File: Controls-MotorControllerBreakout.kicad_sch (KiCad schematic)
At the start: 16 parts, among them J1 MC CAN 1, J2 MC CAN 2, J3 CAN INTRFC, J4 EXT PWR, J5 CANDAPTER, Q1 PMV35EPER

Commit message: gerbs + bom
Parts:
- J5: P/N (none) -> L77SDE09SA4CH3R
- Q1: P/N (none) -> PMV35EPER
- Z1: P/N (none) -> BZT52-B12-QX

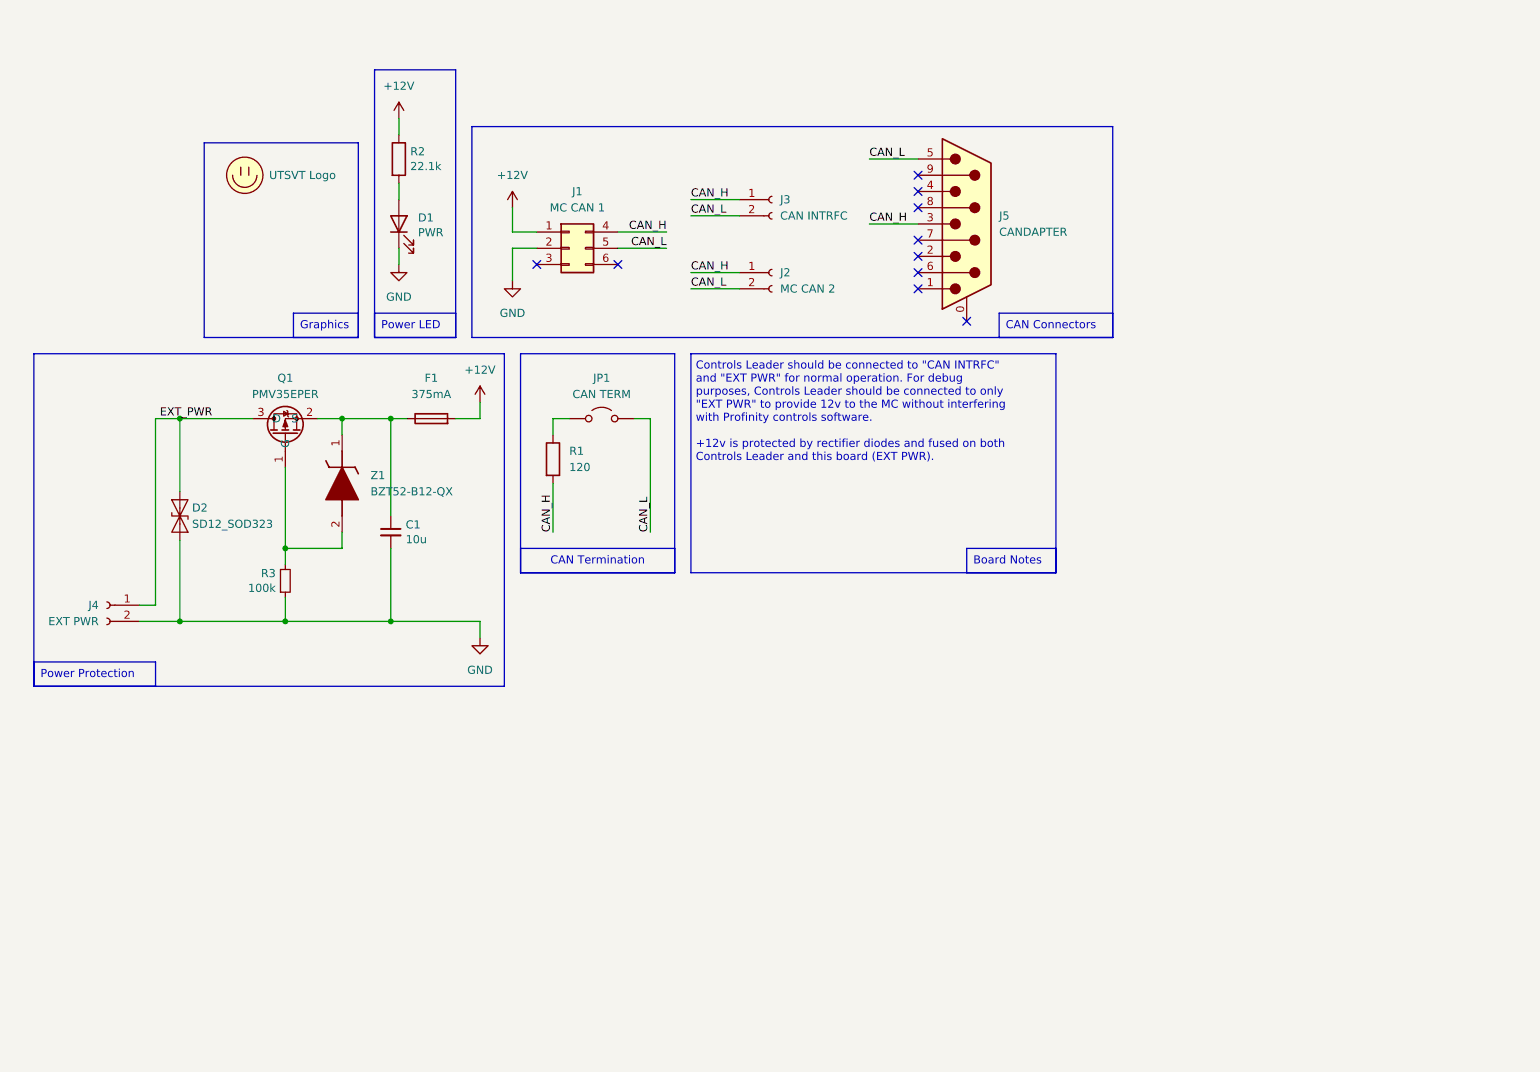
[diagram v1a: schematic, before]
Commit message: separate connector for controls
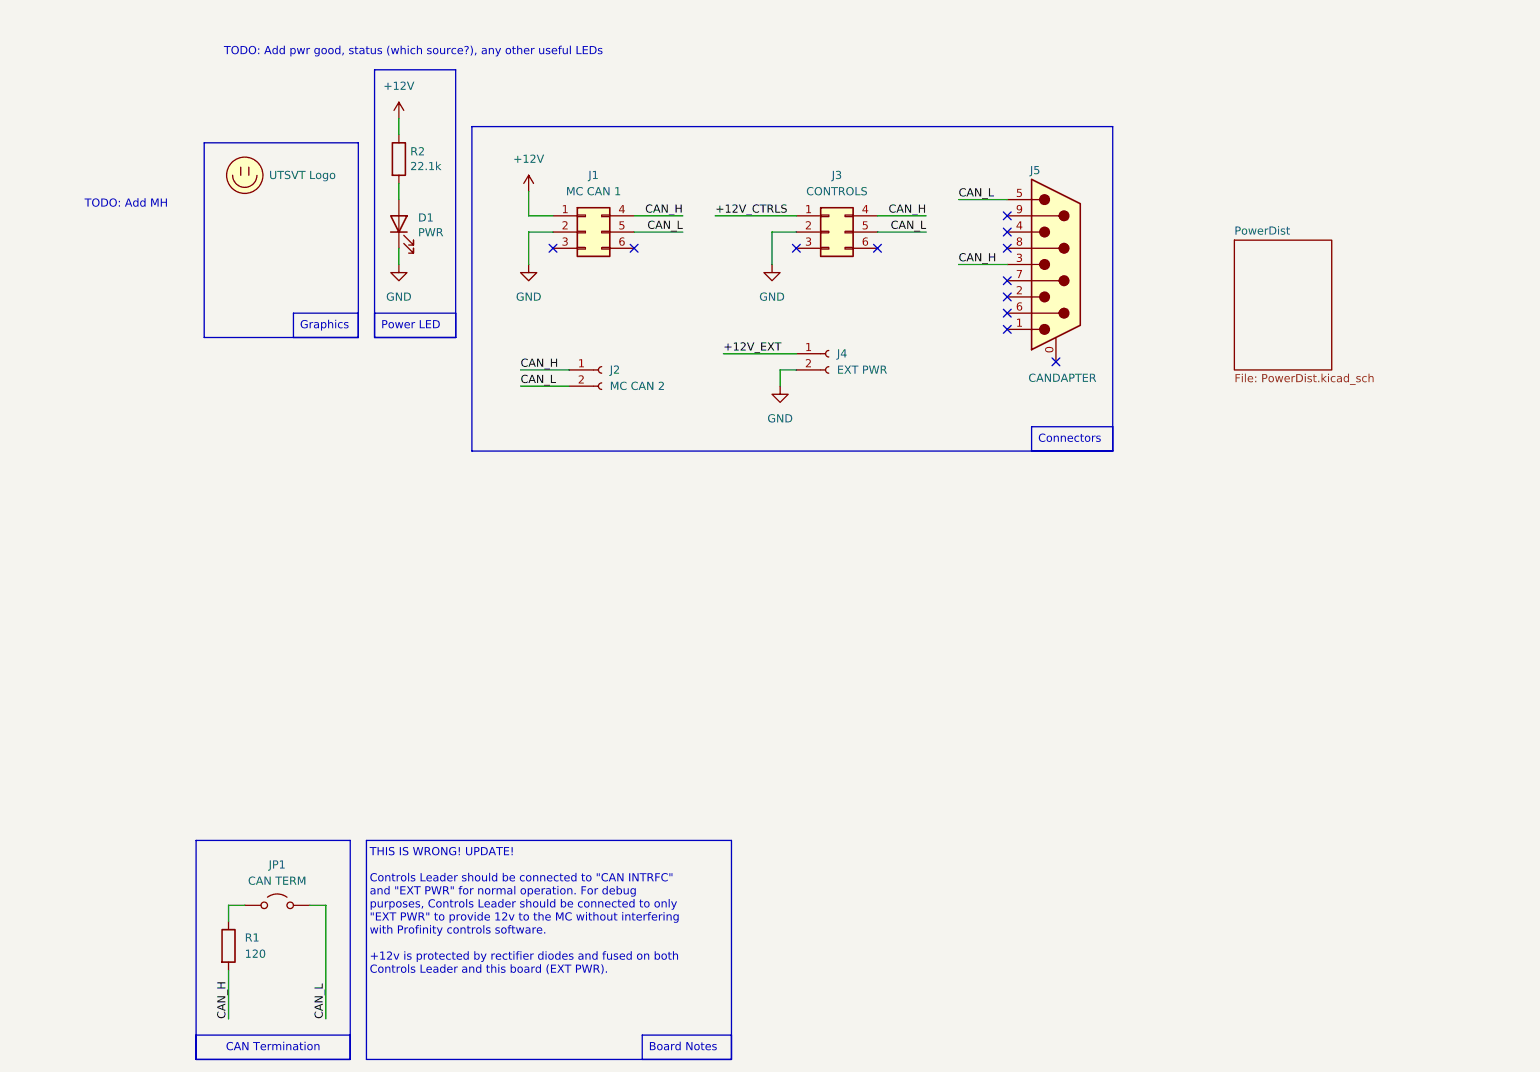
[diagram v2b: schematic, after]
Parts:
- removed C1: 10u, Capacitor_SMD:C_0805_2012Metric, symbol Device:C_Small
- removed D2: SD12_SOD323, Diode_SMD:D_SOD-323, symbol Diode:SD12_SOD323
- removed F1: 375mA, Fuse:Fuse_1206_3216Metric, symbol Device:Fuse
- removed J3: CAN INTRFC, Connector_Molex:Molex_Micro-Fit_3.0_43650-0215_1x02_P3.00mm_Vertical, symbol Connector:Conn_01x02_Socket
- removed Q1: PMV35EPER, Package_TO_SOT_SMD:SOT-23, symbol utsvt-chips:PMV35EPE
- removed R3: 100k, Resistor_SMD:R_0805_2012Metric_Pad1.20x1.40mm_HandSolder, symbol Device:R_Small
- removed Z1: BZT52-B12-QX, Zener:BZT52B12QX, symbol BZT52-B12-QX:BZT52-B12-QX
- added J3: CONTROLS, Connector_Molex:Molex_Micro-Fit_3.0_43045-0612_2x03_P3.00mm_Vertical, symbol Connector_Generic:Conn_02x03_Top_Bottom
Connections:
- net CAN_H: now also J3.4 (Pin_4)
- net CAN_L: now also J3.5 (Pin_5)
- net GND: now also J3.2 (Pin_2)
- net EXT_PWR renamed +12V_EXT
- new net +12V_CTRLS: J3.1 (Pin_1)
- no-connect marks 10 -> 12
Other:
- added sheet PowerDist (PowerDist.kicad_sch)
- note added: "THIS IS WRONG! UPDATE! Controls Leader should be connected to "CAN INTRFC" and "EXT PWR" for normal operation. For debug purposes, Controls Leader should be connected to only "EXT PWR" to provide 12v to the MC without interfering with Profinity controls software. +12v is protected by rectifier diodes and fused on both Controls Leader and this board (EXT PWR)."
- note added: "TODO: Add MH"
- note added: "TODO: Add pwr good, status (which source?), any other useful LEDs"
- note removed: "Controls Leader should be connected to "CAN INTRFC" and "EXT PWR" for normal operation. For debug purposes, Controls Leader should be connected to only "EXT PWR" to provide 12v to the MC without interfering with Profinity controls software. +12v is protected by rectifier diodes and fused on both Controls Leader and this board (EXT PWR)."
- company: (none) -> LHRS
- title: (none) -> Controls - Motor Controller Breakout
- moved on the sheet: J1, J2, J5, JP1, R1

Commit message: sch is sching (tps2121 design)
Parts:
- added H1, H2, H3, H4: MountingHole, symbol Mechanical:MountingHole
- J3: value CONTROLS -> CTRLS
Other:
- sheet PowerDist ports: added +12V_CTRLS, +12V_EXT, +12V_STATUS; removed none
- note removed: "TODO: Add MH"
- moved on the sheet: D1, R2

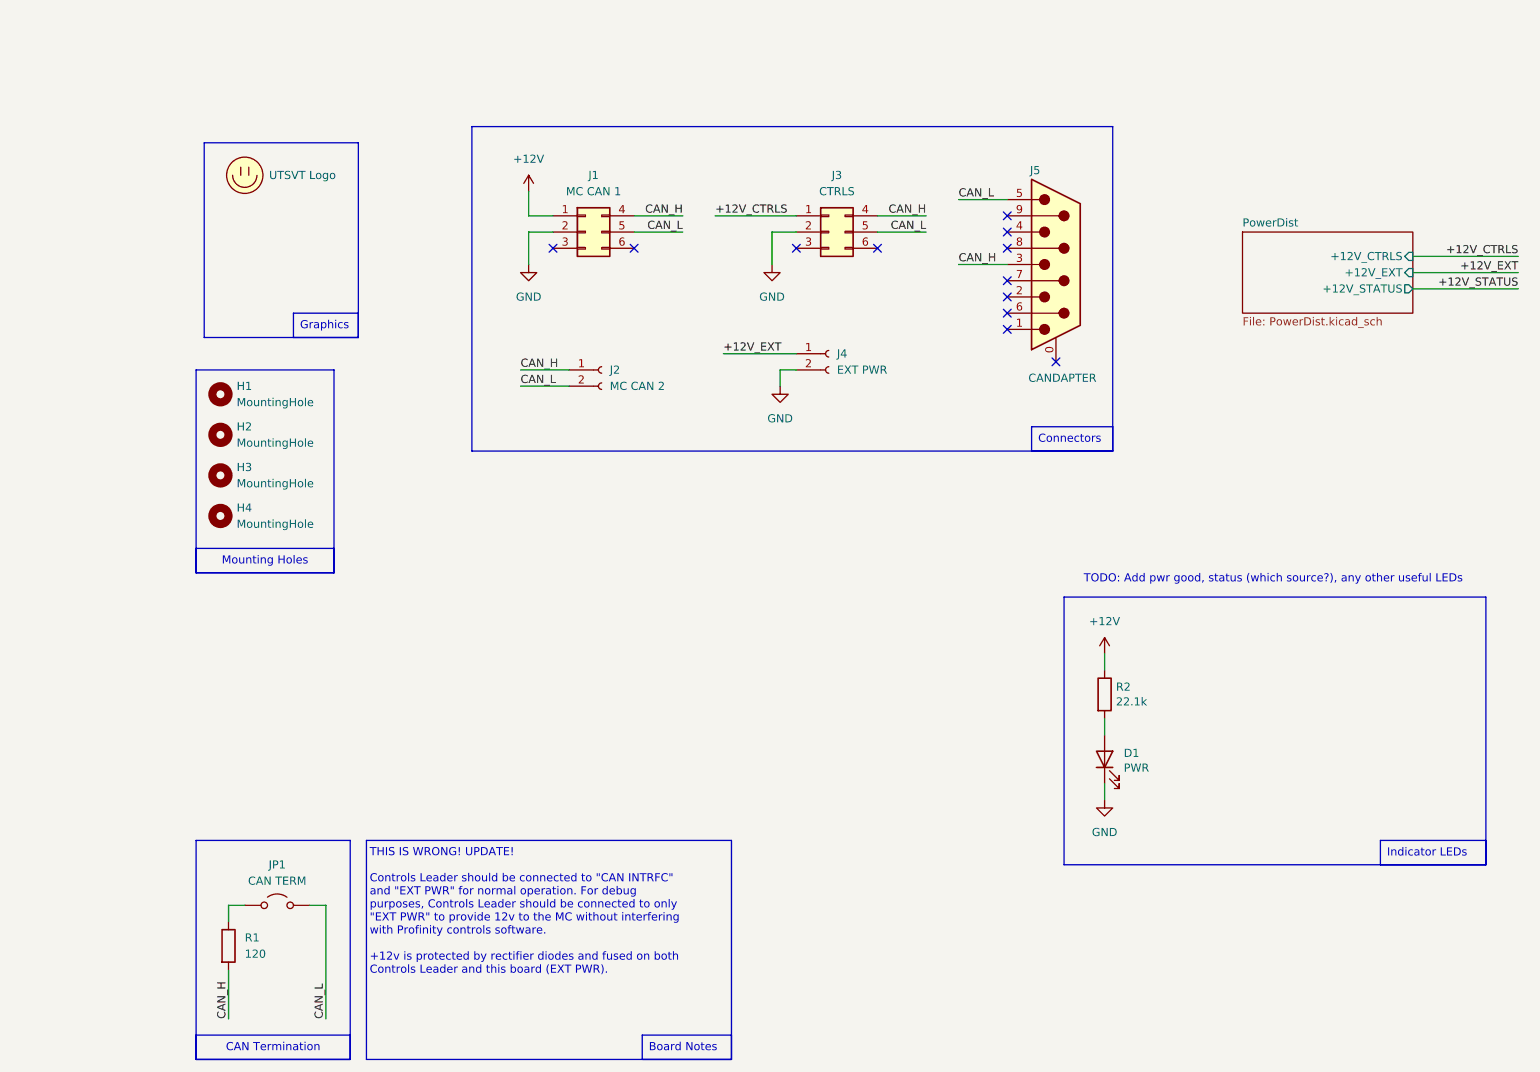
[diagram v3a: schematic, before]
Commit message: cleanup sch and add leds
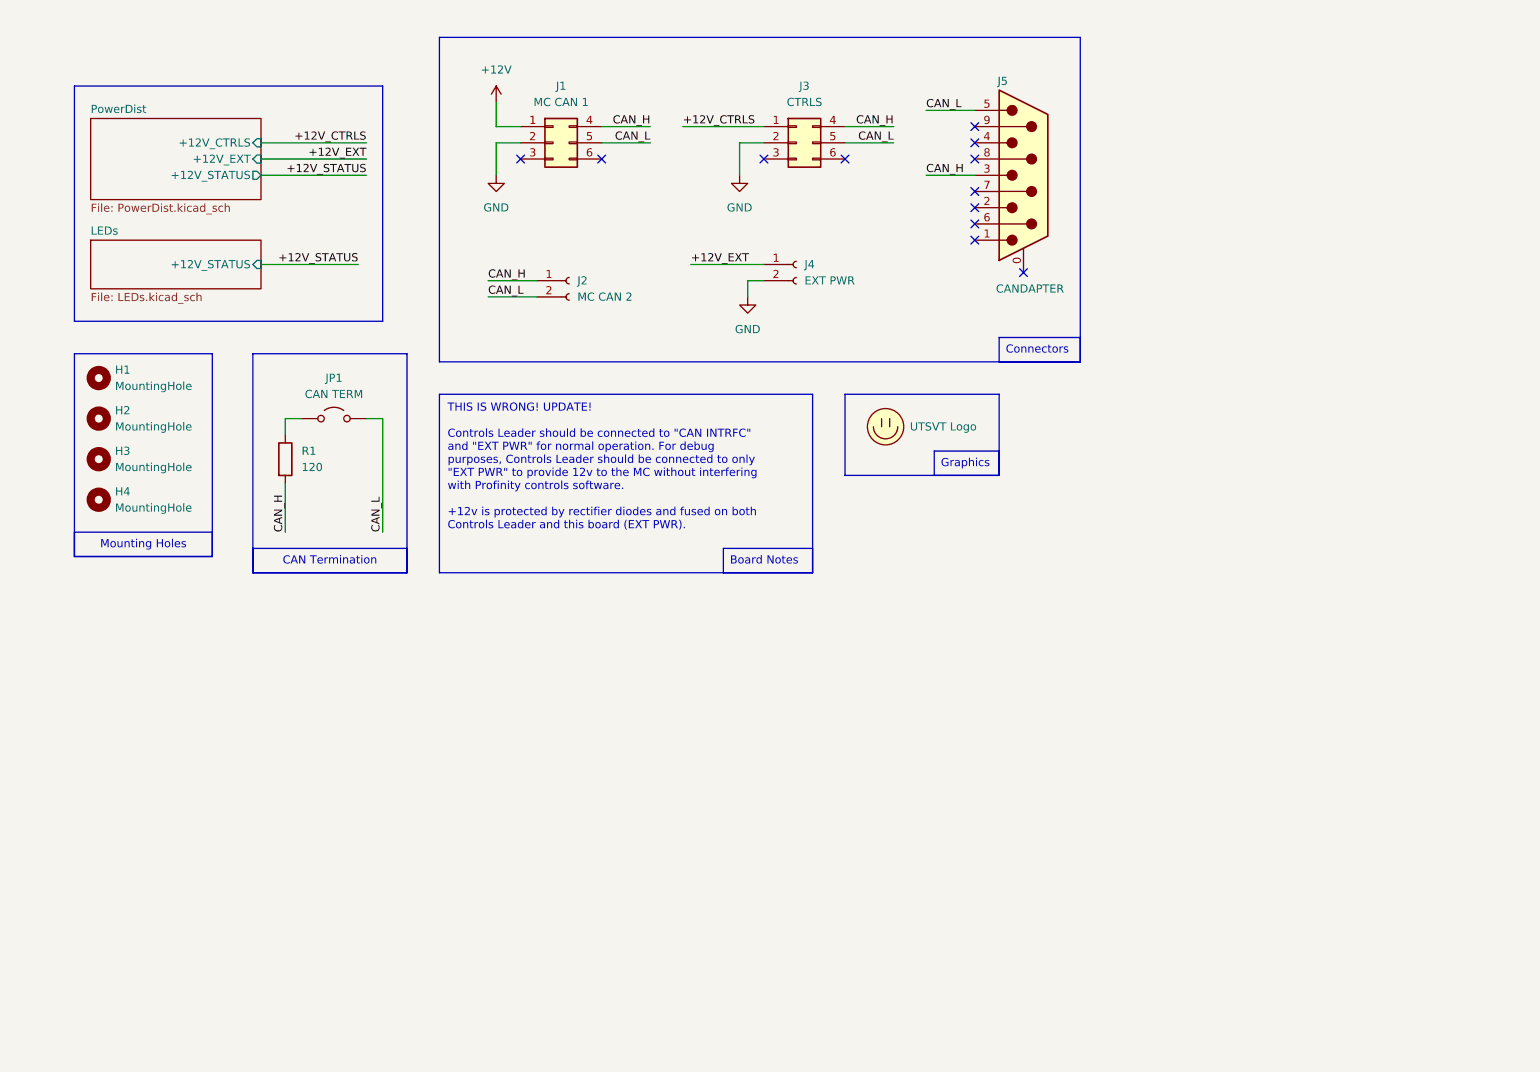
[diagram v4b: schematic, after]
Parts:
- removed D1: PWR, LED_SMD:LED_0805_2012Metric, symbol Device:LED
- removed R2: 22.1k, Resistor_SMD:R_0805_2012Metric, symbol Device:R
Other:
- added sheet LEDs (LEDs.kicad_sch)
- note removed: "TODO: Add pwr good, status (which source?), any other useful LEDs"
- moved on the sheet: H1, H2, H3, H4, J1, J2, J3, J4, J5, JP1, R1

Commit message: layout kinda screwy but it works?
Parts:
- added LOGO2: Hallock, UTSVT_Special:Hallock_Image_Tiny, symbol utsvt-misc:Logo_Placeholder
- H1, H2, H3, H4: footprint (none) -> MountingHole:MountingHole_3mm
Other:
- note added: "TODO: add testpoints and stuff"
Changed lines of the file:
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@@
 	(rectangle
 		(start 140.97 73.66)
-		(end 165.1 86.36)
+		(end 165.1 101.6)
 		(stroke
 			(width 0)
@@
 	(text_box "Graphics"
 		(exclude_from_sim no)
-		(at 154.94 82.55 0)
+		(at 154.94 97.79 0)
 		(size 10.16 3.81)
 		(stroke
@@
 			)
 			(justify top)
+		)
+	)
+	(text "TODO: add testpoints and stuff"
+		(exclude_from_sim no)
+		(at 29.21 15.494 0)
+		(effects
+			(font
+				(size 1.27 1.27)
+			)
 		)
 	)
@@
 			)
 		)
-		(property "Footprint" ""
+		(property "Footprint" "MountingHole:MountingHole_3mm"
 			(at 24.13 83.82 0)
 			(effects
@@
 				(path "/0a971d65-5373-49c6-bc07-3a5d4263dbef"
 					(reference "H3")
+					(unit 1)
+				)
+			)
+		)
+	)
+	(symbol
+		(lib_id "utsvt-misc:Logo_Placeholder")
+		(at 147.32 86.36 0)
+		(unit 1)
+		(exclude_from_sim no)
+		(in_bom yes)
+		(on_board yes)
+		(dnp no)
+		(fields_autoplaced yes)
+		(property "Reference" "LOGO2"
+			(at 147.32 82.55 0)
+			(effects
+				(font
+					(size 1.27 1.27)
+				)
+				(hide yes)
+			)
+		)
+		(property "Value" "Hallock"
+			(at 151.13 86.3599 0)
+			(effects
+				(font
+					(size 1.27 1.27)
+				)
+				(justify left)
+			)
+		)
+		(property "Footprint" "UTSVT_Special:Hallock_Image_Tiny"
+			(at 147.32 84.455 0)
+			(effects
+				(font
+					(size 1.27 1.27)
+				)
+				(hide yes)
+			)
+		)
+		(property "Datasheet" ""
+			(at 147.32 84.455 0)
+			(effects
+				(font
+					(size 1.27 1.27)
+				)
+				(hide yes)
+			)
+		)
+		(property "Description" "Graph footprint placeholder"
+			(at 147.32 86.36 0)
+			(effects
+				(font
+					(size 1.27 1.27)
+				)
+				(hide yes)
+			)
+		)
+		(instances
+			(project ""
+				(path "/0a971d65-5373-49c6-bc07-3a5d4263dbef"
+					(reference "LOGO2")
 					(unit 1)
 				)
@@
 			)
 		)
-		(property "Footprint" ""
+		(property "Footprint" "MountingHole:MountingHole_3mm"
 			(at 24.13 71.12 0)
 			(effects
@@
 			)
 		)
-		(property "Datasheet" "~"
+		(property "Datasheet" "https://cdn.amphenol-cs.com/media/wysiwyg/files/drawing/l77sdxxxsa4ch3r.pdf"
 			(at 168.91 39.37 0)
 			(effects
@@
 			)
 		)
-		(property "Footprint" ""
+		(property "Footprint" "MountingHole:MountingHole_3mm"
 			(at 24.13 77.47 0)
 			(effects
@@
 			)
 		)
-		(property "Footprint" ""
+		(property "Footprint" "MountingHole:MountingHole_3mm"
 			(at 24.13 90.17 0)
 			(effects

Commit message: initial layout
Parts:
- removed LOGO2: Hallock, UTSVT_Special:Hallock_Image_Tiny, symbol utsvt-misc:Logo_Placeholder
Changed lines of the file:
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@@
-	)
-	(symbol
-		(lib_id "utsvt-misc:Logo_Placeholder")
-		(at 147.32 86.36 0)
-		(unit 1)
-		(exclude_from_sim no)
-		(in_bom yes)
-		(on_board yes)
-		(dnp no)
-		(fields_autoplaced yes)
-		(property "Reference" "LOGO2"
-			(at 147.32 82.55 0)
-			(effects
-				(font
-					(size 1.27 1.27)
-				)
-				(hide yes)
-			)
-		)
-		(property "Value" "Hallock"
-			(at 151.13 86.3599 0)
-			(effects
-				(font
-					(size 1.27 1.27)
-				)
-				(justify left)
-			)
-		)
-		(property "Footprint" "UTSVT_Special:Hallock_Image_Tiny"
-			(at 147.32 84.455 0)
-			(effects
-				(font
-					(size 1.27 1.27)
-				)
-				(hide yes)
-			)
-		)
-		(property "Datasheet" ""
-			(at 147.32 84.455 0)
-			(effects
-				(font
-					(size 1.27 1.27)
-				)
-				(hide yes)
-			)
-		)
-		(property "Description" "Graph footprint placeholder"
-			(at 147.32 86.36 0)
-			(effects
-				(font
-					(size 1.27 1.27)
-				)
-				(hide yes)
-			)
-		)
-		(instances
-			(project ""
-				(path "/0a971d65-5373-49c6-bc07-3a5d4263dbef"
-					(reference "LOGO2")
-					(unit 1)
-				)
-			)
-		)
 	)
 	(symbol
